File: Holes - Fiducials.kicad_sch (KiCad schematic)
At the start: 4 parts

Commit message: Rename the project to OPEN_PHASE
PhaseSense-8586 was named after the first parts of the design (INA240 +
ADS8586S), which are no longer on the board. OPEN_PHASE follows
OPEN_WEIGHT, the other OPEN THRUST LAB board.

- project files: OPEN_PHASE.kicad_pro / _sch / _pcb / _prl / _dru
- libraries: lib/lib_sym/OPEN_PHASE.kicad_sym and
  lib/lib_fp/OPEN_PHASE.pretty, nickname OPEN_PHASE in both tables, in
  every lib_id and in every footprint of the PCB
- project name of every symbol and sheet instance, so the reference
  designators are kept
- PROJECT_NAME and GIT_URL in the project and in kibot_main.yaml, README
  and its template, CHANGELOG, LTspice headers and their generator
- the README note now says the project was first published as
  PhaseSense-8586

The GitHub repository is now foukouda/OPEN_PHASE. The board name
PHASETRACKER is unchanged. The netlist, ERC and DRC reports are the same
before and after the rename.

Co-Authored-By: Claude Opus 5.5 <noreply@anthropic.com>
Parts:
- H1, H2, H3, H4: footprint PhaseSense-8586:MountingHole_3.2mm_M3_Pad_Via -> OPEN_PHASE:MountingHole_3.2mm_M3_Pad_Via; symbol PhaseSense-8586:MountingHole_Pad -> OPEN_PHASE:MountingHole_Pad
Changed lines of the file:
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@@
 		)
 		(instances
-			(project "PhaseSense-8586"
+			(project "OPEN_PHASE"
 				(path "/f9e05184-c88b-4a88-ae9c-ab2bdb32be7c/c5103ceb-5325-4a84-a025-9638a412984e/b825b9f2-4a7b-44ab-b000-02167519e5f9"
 					(reference "#PWR02")
@@
 	)
 	(symbol
-		(lib_id "PhaseSense-8586:MountingHole_Pad")
+		(lib_id "OPEN_PHASE:MountingHole_Pad")
 		(at 156.21 74.93 0)
 		(unit 1)
@@
 			)
 		)
-		(property "Footprint" "PhaseSense-8586:MountingHole_3.2mm_M3_Pad_Via"
+		(property "Footprint" "OPEN_PHASE:MountingHole_3.2mm_M3_Pad_Via"
 			(at 156.21 74.93 0)
 			(hide yes)
@@
 		)
 		(instances
-			(project "PhaseSense-8586"
+			(project "OPEN_PHASE"
 				(path "/f9e05184-c88b-4a88-ae9c-ab2bdb32be7c/c5103ceb-5325-4a84-a025-9638a412984e/b825b9f2-4a7b-44ab-b000-02167519e5f9"
 					(reference "H1")
@@
 	)
 	(symbol
-		(lib_id "PhaseSense-8586:MountingHole_Pad")
+		(lib_id "OPEN_PHASE:MountingHole_Pad")
 		(at 179.07 74.93 0)
 		(unit 1)
@@
 			)
 		)
-		(property "Footprint" "PhaseSense-8586:MountingHole_3.2mm_M3_Pad_Via"
+		(property "Footprint" "OPEN_PHASE:MountingHole_3.2mm_M3_Pad_Via"
 			(at 179.07 74.93 0)
 			(hide yes)
@@
 		)
 		(instances
-			(project "PhaseSense-8586"
+			(project "OPEN_PHASE"
 				(path "/f9e05184-c88b-4a88-ae9c-ab2bdb32be7c/c5103ceb-5325-4a84-a025-9638a412984e/b825b9f2-4a7b-44ab-b000-02167519e5f9"
 					(reference "H4")
@@
 	)
 	(symbol
-		(lib_id "PhaseSense-8586:MountingHole_Pad")
+		(lib_id "OPEN_PHASE:MountingHole_Pad")
 		(at 163.83 74.93 0)
 		(unit 1)
@@
 			)
 		)
-		(property "Footprint" "PhaseSense-8586:MountingHole_3.2mm_M3_Pad_Via"
+		(property "Footprint" "OPEN_PHASE:MountingHole_3.2mm_M3_Pad_Via"
 			(at 163.83 74.93 0)
 			(hide yes)
@@
 		)
 		(instances
-			(project "PhaseSense-8586"
+			(project "OPEN_PHASE"
 				(path "/f9e05184-c88b-4a88-ae9c-ab2bdb32be7c/c5103ceb-5325-4a84-a025-9638a412984e/b825b9f2-4a7b-44ab-b000-02167519e5f9"
 					(reference "H2")
@@
 	)
 	(symbol
-		(lib_id "PhaseSense-8586:MountingHole_Pad")
+		(lib_id "OPEN_PHASE:MountingHole_Pad")
 		(at 171.45 74.93 0)
 		(unit 1)
@@
 			)
 		)
-		(property "Footprint" "PhaseSense-8586:MountingHole_3.2mm_M3_Pad_Via"
+		(property "Footprint" "OPEN_PHASE:MountingHole_3.2mm_M3_Pad_Via"
 			(at 171.45 74.93 0)
 			(hide yes)
@@
 		)
 		(instances
-			(project "PhaseSense-8586"
+			(project "OPEN_PHASE"
 				(path "/f9e05184-c88b-4a88-ae9c-ab2bdb32be7c/c5103ceb-5325-4a84-a025-9638a412984e/b825b9f2-4a7b-44ab-b000-02167519e5f9"
 					(reference "H3")

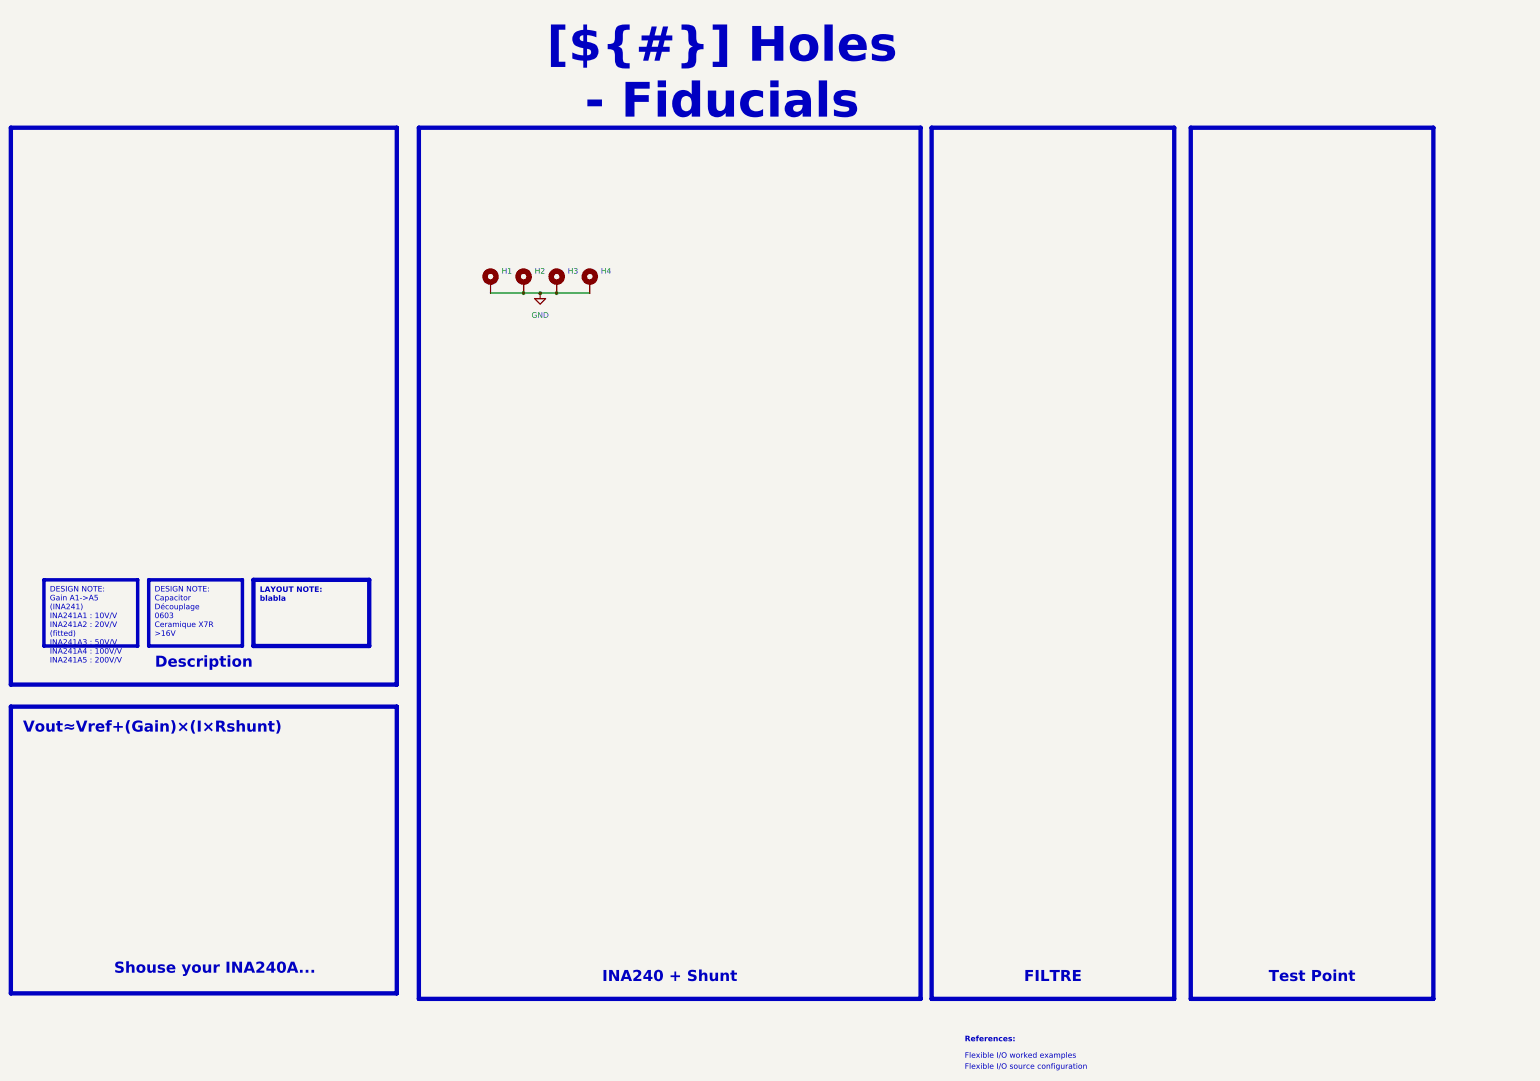
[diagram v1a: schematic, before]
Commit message: Restyle schematic sheets, new title block logo, WE-MAPI inductor in simulations
- Schematic sheets: restyled frames, tables and text boxes
- Title block: INGENIERIE FRANCE logo in KDT_Template_GIT.kicad_wks
- LTspice: L1 modelled as WE-MAPI 4030 74438357022 (22 mOhm),
  simulations 01 and 03 rerun, README and results updated

Co-Authored-By: Claude Opus 5.5 <noreply@anthropic.com>
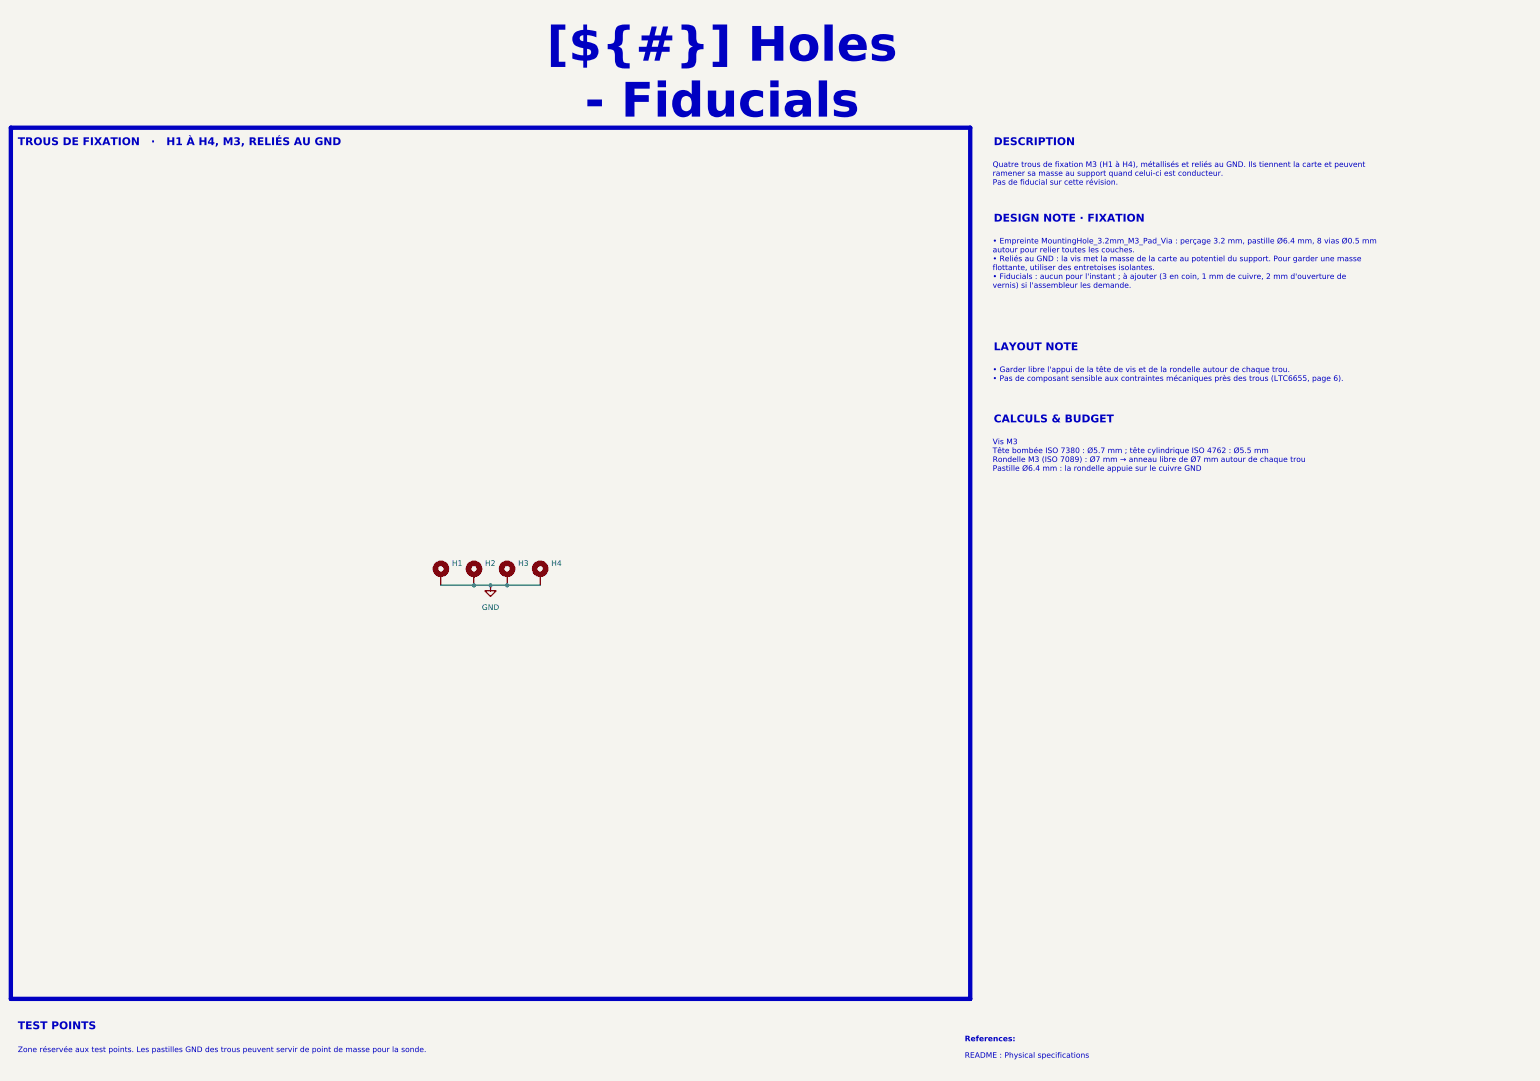
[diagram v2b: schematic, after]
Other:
- note added: "README : Physical specifications"
- note removed: "Flexible I/O source configuration"
- note removed: "Flexible I/O worked examples"
- note removed: "Vout≈Vref+(Gain)×(I×Rshunt)"
- moved on the sheet: H1, H2, H3, H4
